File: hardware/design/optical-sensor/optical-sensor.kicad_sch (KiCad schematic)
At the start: 9 parts, among them U1 CNY70

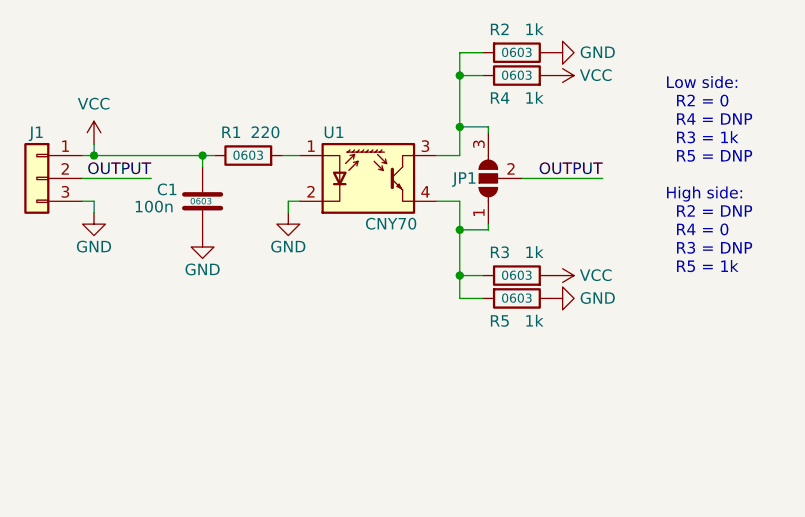
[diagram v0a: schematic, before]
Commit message: Added Hall sensor position on PCB
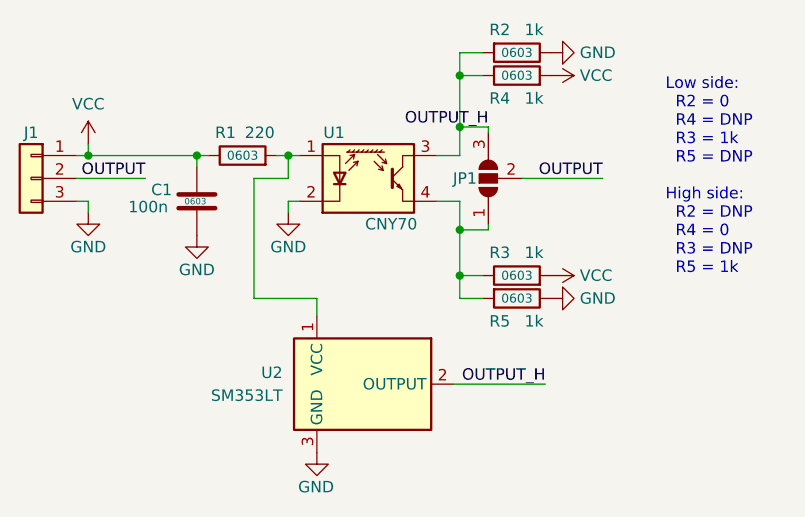
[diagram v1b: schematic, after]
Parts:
- added U2: SM353LT, Package_TO_SOT_SMD:SOT-23, symbol Sensor_Magnetic:SM353LT
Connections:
- net GND: now also U2.3 (GND)
- net OUTPUT_H: now reaches JP1.3 (B), R2.2, R4.1, U1.3 (C)
- net OUTPUT_H: now also U2.2 (OUTPUT)
- net at R1.2, U1.1 (A): now also U2.1 (VCC)
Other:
- moved on the sheet: C1, J1, R1
